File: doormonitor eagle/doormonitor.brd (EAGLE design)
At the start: 38.6 x 38.6 mm, 12 parts, among them U1 ATTINY84, Y1 8MHz

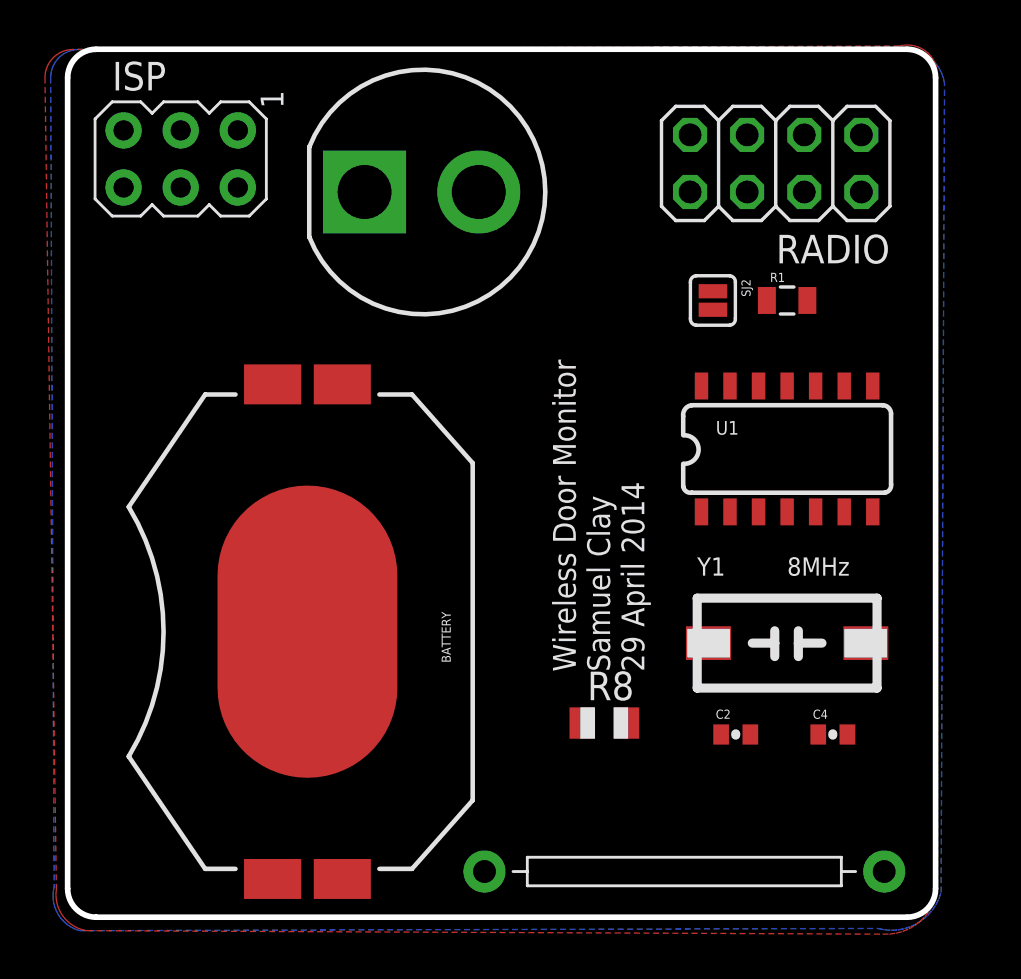
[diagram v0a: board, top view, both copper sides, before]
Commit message: Board layout. Includes optional JST connector.
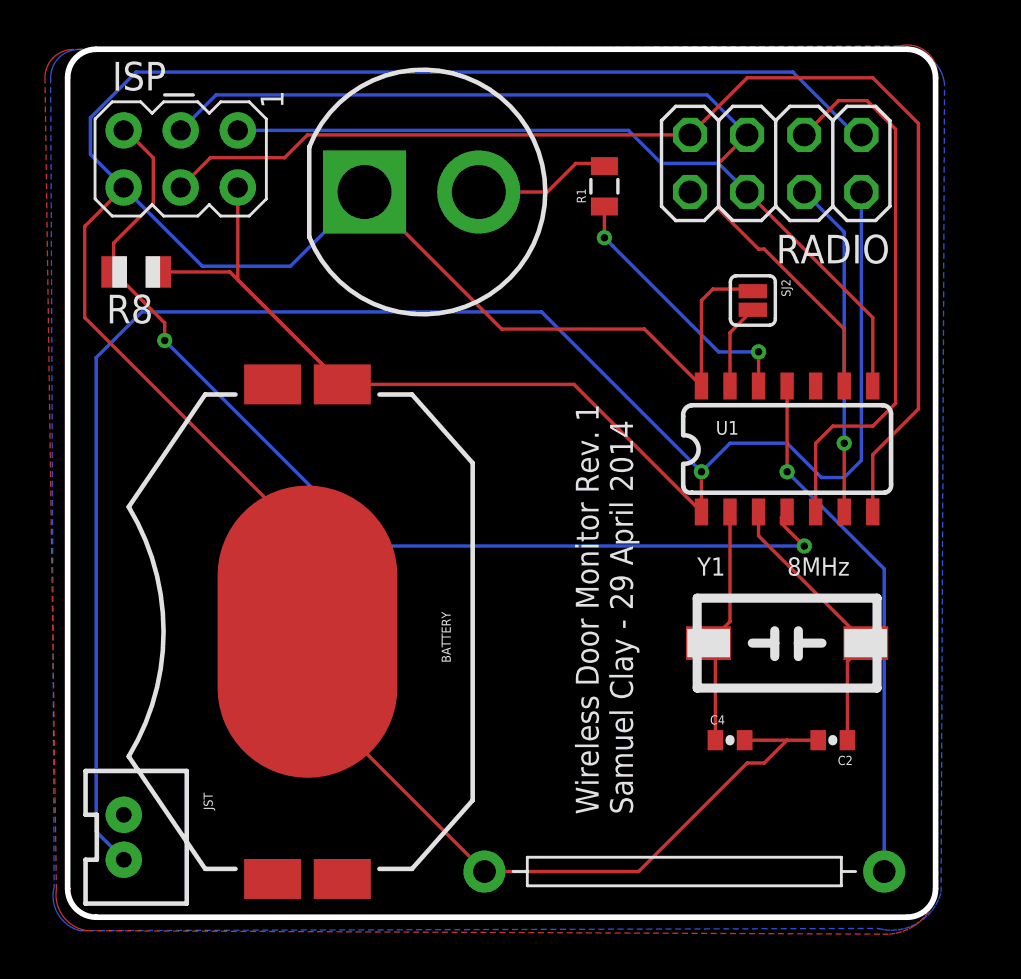
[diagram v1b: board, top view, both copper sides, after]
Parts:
- added JST: BATT, SparkFun-Connectors:JST-2-PTH-VERT
- moved R8 28.9 mm to (3.05, 28.7), turned to 180 degrees
- moved R1 9.58 mm to (23.9, 32.5), turned to 90 degrees
- moved C4 4.58 mm to (29.5, 7.87)
- moved C2 4.33 mm to (34.0, 7.87), turned to 180 degrees
- moved SJ2 1.78 mm to (30.5, 27.4)
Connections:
- net GND: now also JST.1
- net VCC: now also JST.2
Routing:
- net GND: track 0.00 -> 136.1 mm
- net VCC: track 0.00 -> 115.1 mm, vias 0 -> 1
- net MOSI: track 0.00 -> 53.8 mm
- net RESET: track 0.00 -> 45.9 mm, vias 0 -> 2
- net SCK: track 0.00 -> 40.7 mm
- net MISO: track 0.00 -> 34.7 mm
- net CE: track 0.00 -> 24.8 mm
- net REED: track 0.00 -> 23.4 mm, vias 0 -> 1
- net CSN: track 0.00 -> 15.0 mm, vias 0 -> 1
- net N$3: track 0.00 -> 12.5 mm
- net LED: track 0.00 -> 11.9 mm, vias 0 -> 2
- net N$4: track 0.00 -> 10.7 mm
- net N$6: track 0.00 -> 6.16 mm
- net N$2: track 0.00 -> 3.81 mm
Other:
- board text added: "Wireless Door Monitor Rev. 1 Samuel Clay - 29 April 2014"
- board text removed: "Wireless Door Monitor Samuel Clay 29 April 2014"

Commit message: Updating schematic.
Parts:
- renumbered SJ2 to SJ1, U1 to MCU
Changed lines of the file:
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@@
 <element name="C2" library="SparkFun-Passives" package="0402-CAP" value="18pF" x="34.036" y="7.874" rot="R180"/>
 <element name="C4" library="SparkFun-Passives" package="0402-CAP" value="18pF" x="29.464" y="7.874"/>
-<element name="SJ2" library="SparkFun-Passives" package="SJ_2S" value="Receiver?" x="30.48" y="27.432" rot="R270"/>
-<element name="U1" library="SparkFun-DigitalIC" package="SO14" value="ATTINY84" x="32.004" y="20.828"/>
+<element name="SJ1" library="SparkFun-Passives" package="SJ_2S" value="Receiver?" x="30.48" y="27.432" rot="R270"/>
+<element name="MCU" library="SparkFun-DigitalIC" package="SO14" value="ATTINY84" x="32.004" y="20.828"/>
 <element name="S1" library="SparkFun-Electromechanical" package="REED_SWITCH_PTH" value="REED SWITCH" x="27.432" y="2.032" rot="R180"/>
 <element name="Y1" library="remote" package="NX8045GB" value="8MHz" x="32.004" y="12.192"/>
@@
 <contactref element="ISP" pad="6"/>
 <contactref element="RADIO" pad="1"/>
-<contactref element="U1" pad="14"/>
+<contactref element="MCU" pad="14"/>
 <contactref element="C4" pad="2"/>
 <contactref element="C2" pad="2"/>
-<contactref element="SJ2" pad="1"/>
+<contactref element="SJ1" pad="1"/>
 <contactref element="BATTERY" pad="2"/>
 <contactref element="S1" pad="P$2"/>
@@
 <contactref element="ISP" pad="1"/>
 <contactref element="RADIO" pad="6"/>
-<contactref element="U1" pad="8"/>
+<contactref element="MCU" pad="8"/>
 <wire x1="35.814" y1="23.628" x2="35.814" y2="26.67" width="0.1524" layer="1"/>
 <wire x1="35.814" y1="26.67" x2="30.226" y2="32.258" width="0.1524" layer="1"/>
@@
 <contactref element="ISP" pad="4"/>
 <contactref element="RADIO" pad="7"/>
-<contactref element="U1" pad="7"/>
+<contactref element="MCU" pad="7"/>
 <wire x1="35.814" y1="18.028" x2="35.814" y2="20.574" width="0.1524" layer="1"/>
 <wire x1="35.814" y1="20.574" x2="37.846" y2="22.606" width="0.1524" layer="1"/>
@@
 <contactref element="ISP" pad="3"/>
 <contactref element="RADIO" pad="5"/>
-<contactref element="U1" pad="9"/>
+<contactref element="MCU" pad="9"/>
 <wire x1="34.544" y1="23.628" x2="34.544" y2="26.162" width="0.1524" layer="1"/>
 <wire x1="34.544" y1="26.162" x2="30.988" y2="29.718" width="0.1524" layer="1"/>
@@
 <contactref element="RADIO" pad="2"/>
 <contactref element="R8" pad="1"/>
-<contactref element="U1" pad="1"/>
+<contactref element="MCU" pad="1"/>
 <contactref element="BATTERY" pad="1"/>
 <wire x1="12.218" y1="23.7" x2="22.522" y2="23.7" width="0.1524" layer="1"/>
@@
 <contactref element="ISP" pad="5"/>
 <contactref element="R8" pad="2"/>
-<contactref element="U1" pad="4"/>
+<contactref element="MCU" pad="4"/>
 <wire x1="2.49" y1="34.998" x2="2.594" y2="34.998" width="0.1524" layer="1"/>
 <wire x1="2.594" y1="34.998" x2="3.81" y2="33.782" width="0.1524" layer="1"/>
@@
 <signal name="CE">
 <contactref element="RADIO" pad="3"/>
-<contactref element="U1" pad="5"/>
+<contactref element="MCU" pad="5"/>
 <wire x1="33.274" y1="18.028" x2="33.274" y2="21.082" width="0.1524" layer="1"/>
 <wire x1="33.274" y1="21.082" x2="34.036" y2="21.844" width="0.1524" layer="1"/>
@@
 <signal name="CSN">
 <contactref element="RADIO" pad="4"/>
-<contactref element="U1" pad="6"/>
+<contactref element="MCU" pad="6"/>
 <wire x1="34.544" y1="18.028" x2="34.544" y2="21.082" width="0.1524" layer="1"/>
 <via x="34.544" y="21.082" extent="1-16" drill="0.3302"/>
@@
 </signal>
 <signal name="RST">
-<contactref element="U1" pad="10"/>
+<contactref element="MCU" pad="10"/>
 </signal>
 <signal name="N$3">
-<contactref element="U1" pad="3"/>
+<contactref element="MCU" pad="3"/>
 <contactref element="C2" pad="1"/>
 <contactref element="Y1" pad="P$2"/>
@@
 </signal>
 <signal name="N$4">
-<contactref element="U1" pad="2"/>
+<contactref element="MCU" pad="2"/>
 <contactref element="C4" pad="1"/>
 <contactref element="Y1" pad="P$1"/>
@@
 </signal>
 <signal name="N$2">
-<contactref element="U1" pad="13"/>
-<contactref element="SJ2" pad="2"/>
+<contactref element="MCU" pad="13"/>
+<contactref element="SJ1" pad="2"/>
 <wire x1="29.464" y1="23.628" x2="29.464" y2="26.0041" width="0.1524" layer="1"/>
 <wire x1="29.464" y1="26.0041" x2="30.48" y2="27.0201" width="0.1524" layer="1"/>
 </signal>
 <signal name="REED">
-<contactref element="U1" pad="11"/>
+<contactref element="MCU" pad="11"/>
 <contactref element="S1" pad="P$1"/>
 <wire x1="36.322" y1="15.494" x2="32.004" y2="19.812" width="0.1524" layer="16"/>
@@
 </signal>
 <signal name="LED">
-<contactref element="U1" pad="12"/>
+<contactref element="MCU" pad="12"/>
 <contactref element="R1" pad="1"/>
 <wire x1="30.734" y1="23.628" x2="30.734" y2="25.146" width="0.1524" layer="1"/>

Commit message: Removing unused line.
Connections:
- removed net RST: MCU.10
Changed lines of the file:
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@@
 <signal name="N$1">
-</signal>
-<signal name="RST">
-<contactref element="MCU" pad="10"/>
 </signal>
 <signal name="N$3">

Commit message: Fixing pinchange.
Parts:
- removed MCU: ATTINY84, SparkFun-DigitalIC:SO14
- added ATTINY84: (no value), Atmel_By_element14_Batch_1:SOIC127P600X175-14N
- added U$1: VIA, thinkmaketest:FANCYVIA
- C2, C4: device SparkFun-Passives:0402-CAP -> SparkFun-Passives:0805
- LED1: device SparkFun-LED:LED10MM -> led:LED5MM
- moved C4 5.33 mm to (34.8, 7.87), turned to 180 degrees
- moved C2 4.83 mm to (29.2, 7.87), turned to 0 degrees
- moved SJ1 3.14 mm to (27.4, 28.2)
- moved LED1 1.27 mm to (14.5, 32.3), turned to 180 degrees
- moved Y1 0.57 mm to (31.8, 12.7), turned to 180 degrees
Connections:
- net CE: now also ATTINY84.6; no longer MCU.5
- net CSN: now also ATTINY84.10; no longer MCU.6
- net GND: now also ATTINY84.14, LED1.K; no longer LED1.C, MCU.14
- net LED: now also ATTINY84.12; no longer MCU.12
- net MISO: now also ATTINY84.8; no longer MCU.8
- net MOSI: now also ATTINY84.7; no longer MCU.7
- net N$2: now also ATTINY84.13; no longer MCU.13
- net N$3: now also ATTINY84.2, U$1.VIA; no longer MCU.3
- net N$4: now also ATTINY84.3; no longer MCU.2
- net REED: now also ATTINY84.11; no longer MCU.11
- net RESET: now also ATTINY84.4; no longer MCU.4
- net SCK: now also ATTINY84.9; no longer MCU.9
- net VCC: now also ATTINY84.1; no longer MCU.1
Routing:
- net VCC: track 115.1 -> 97.5 mm
- net GND: track 136.1 -> 145.7 mm, vias 0 -> 1
- net CSN: track 15.0 -> 9.07 mm
- net N$3: track 12.5 -> 16.4 mm
- net N$4: track 10.7 -> 14.1 mm
- net N$6: track 6.16 -> 8.70 mm
- net N$2: track 3.81 -> 5.23 mm
- net CE: track 24.8 -> 23.4 mm
- net LED: track 11.9 -> 13.2 mm, vias 2 -> 0
- net RESET: track 45.9 -> 46.0 mm, vias 2 -> 1
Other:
- board text added: "Wireless Door Monitor Rev. 2 Samuel Clay - 27 May 2014"
- board text removed: "Wireless Door Monitor Rev. 1 Samuel Clay - 29 April 2014"
